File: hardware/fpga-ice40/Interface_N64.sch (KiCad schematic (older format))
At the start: 7 parts, among them J6 Conn_02x20_Odd_Even

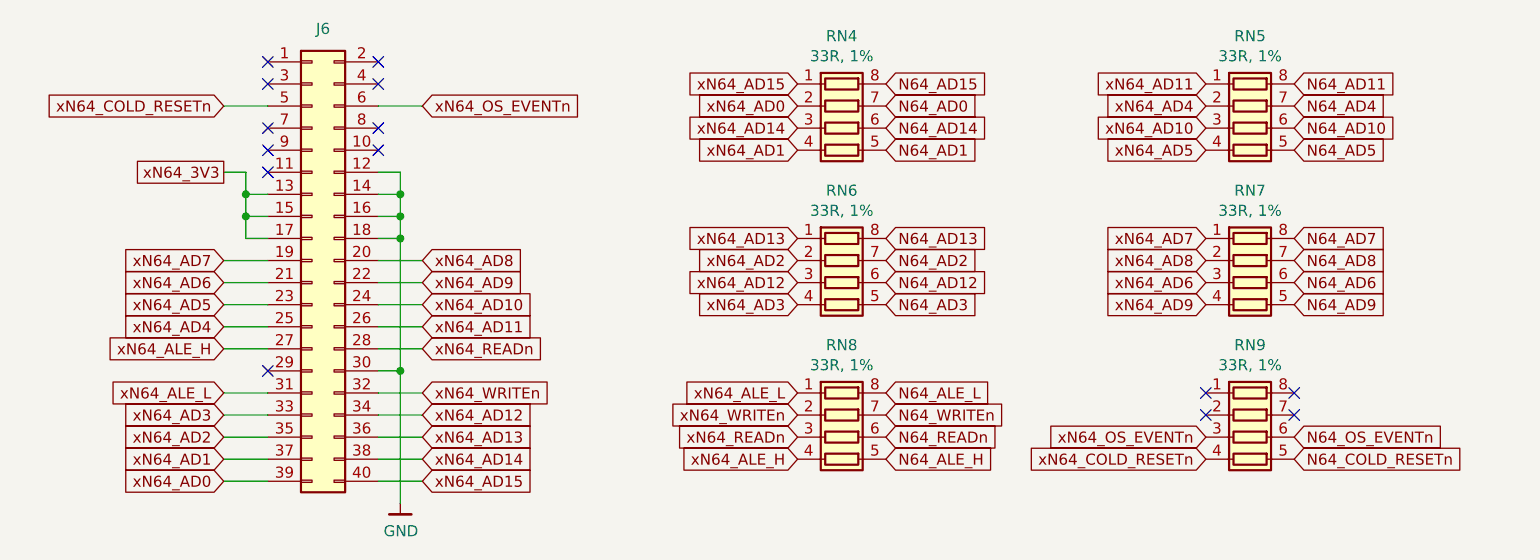
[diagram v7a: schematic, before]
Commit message: Finished routing all nets, including power distribution
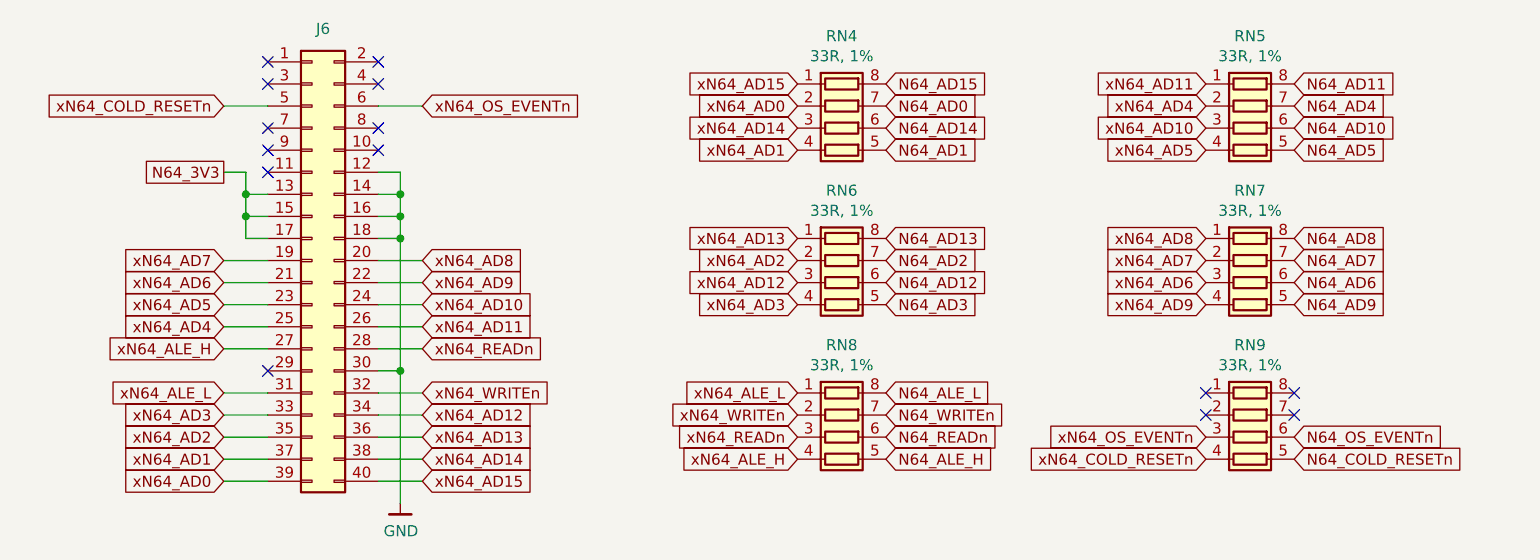
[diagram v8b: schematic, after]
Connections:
- net N64_AD7: now also RN7.7 (R2.2); no longer RN7.8 (R1.2)
- net N64_AD8: now also RN7.8 (R1.2); no longer RN7.7 (R2.2)
- net xN64_AD7: now also RN7.2 (R2.1); no longer RN7.1 (R1.1)
- net xN64_AD8: now also RN7.1 (R1.1); no longer RN7.2 (R2.1)
- net xN64_3V3 renamed N64_3V3
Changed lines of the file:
@@
 xN64_AD15
 Text GLabel 3100 3900 0    50   UnSpc ~ 0
-xN64_3V3
+N64_3V3
 $Comp
 L Device:R_Pack04 RN?
@@
 Text GLabel 7550 4500 0    50   Input ~ 0
 xN64_AD9
-Text GLabel 7550 4300 0    50   Input ~ 0
+Text GLabel 7550 4200 0    50   Input ~ 0
 xN64_AD8
 $Comp
@@
 Text GLabel 7550 4400 0    50   Input ~ 0
 xN64_AD6
-Text GLabel 7550 4200 0    50   Input ~ 0
+Text GLabel 7550 4300 0    50   Input ~ 0
 xN64_AD7
 Text GLabel 6100 3600 2    50   Input ~ 0
@@
 Text GLabel 7950 4500 2    50   Input ~ 0
 N64_AD9
-Text GLabel 7950 4300 2    50   Input ~ 0
+Text GLabel 7950 4200 2    50   Input ~ 0
 N64_AD8
 Text GLabel 7950 5200 2    50   Input ~ 0
@@
 Text GLabel 7950 4400 2    50   Input ~ 0
 N64_AD6
-Text GLabel 7950 4200 2    50   Input ~ 0
+Text GLabel 7950 4300 2    50   Input ~ 0
 N64_AD7
 Wire Wire Line
